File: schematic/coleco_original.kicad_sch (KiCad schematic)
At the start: 6 parts

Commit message: bootup works, controller waits, but no response
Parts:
- added J2: Conn_01x02, Connector_Molex:Molex_KK-254_AE-6410-02A_1x02_P2.54mm_Vertical, symbol Connector_Generic:Conn_01x02
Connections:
- new net GLUE/RX: J2.2 (Pin_2)
- new net GLUE/TX: J2.1 (Pin_1)
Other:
- sheet GLUE ports: added C4_ARM, C7_FIRE, RX, TX; removed none
- sheet controller ports: added C4_ARM, C7_FIRE; removed none
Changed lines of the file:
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@@
+    (stroke (width 0) (type default))
+  )
+  (wire (pts (xy 235.204 109.982) (xy 241.173 109.982))
     (stroke (width 0) (type default))
   )
@@
   )
   (bus (pts (xy 159.258 99.822) (xy 177.165 99.822))
+    (stroke (width 0) (type default))
+  )
+  (wire (pts (xy 235.204 112.141) (xy 241.173 112.141))
     (stroke (width 0) (type default))
   )
@@
         (path "/970e0f64-111f-41e3-9f5a-fb0d0f6fa101"
           (reference "H3") (unit 1)
+        )
+      )
+    )
+  )
+  (symbol (lib_id "Connector_Generic:Conn_01x02") (at 240.284 92.456 0) (unit 1)
+    (in_bom yes) (on_board yes) (dnp no)
+    (property "Reference" "J2" (at 242.316 92.6592 0)
+      (effects (font (size 1.27 1.27)) (justify left))
+    )
+    (property "Value" "Conn_01x02" (at 242.316 94.9706 0)
+      (effects (font (size 1.27 1.27)) (justify left))
+    )
+    (property "Footprint" "Connector_Molex:Molex_KK-254_AE-6410-02A_1x02_P2.54mm_Vertical" (at 240.284 92.456 0)
+      (effects (font (size 1.27 1.27)) hide)
+    )
+    (property "Datasheet" "~" (at 240.284 92.456 0)
+      (effects (font (size 1.27 1.27)) hide)
+    )
+    (pin "1")
+    (pin "2")
+    (instances
+      (project "coleco_original"
+        (path "/970e0f64-111f-41e3-9f5a-fb0d0f6fa101/00000000-0000-0000-0000-000062624749"
+          (reference "J2") (unit 1)
+        )
+        (path "/970e0f64-111f-41e3-9f5a-fb0d0f6fa101"
+          (reference "J9") (unit 1)
+        )
+      )
+      (project "picerino_sn76489AN"
+        (path "/b5352a33-563a-4ffe-a231-2e68fb54afa3"
+          (reference "J2") (unit 1)
         )
       )
@@
       (effects (font (size 1.27 1.27)) (justify left))
     )
+    (pin "RX" input (at 235.204 94.996 0)
+      (effects (font (size 1.27 1.27)) (justify right))
+    )
+    (pin "TX" output (at 235.204 92.456 0)
+      (effects (font (size 1.27 1.27)) (justify right))
+    )
+    (pin "C4_ARM" output (at 235.204 109.982 0)
+      (effects (font (size 1.27 1.27)) (justify right))
+    )
+    (pin "C7_FIRE" output (at 235.204 112.141 0)
+      (effects (font (size 1.27 1.27)) (justify right))
+    )
     (instances
       (project "coleco_original"
@@
       (effects (font (size 1.27 1.27)) (justify left))
     )
+    (pin "C4_ARM" input (at 241.173 109.982 180)
+      (effects (font (size 1.27 1.27)) (justify left))
+    )
+    (pin "C7_FIRE" input (at 241.173 112.141 180)
+      (effects (font (size 1.27 1.27)) (justify left))
+    )

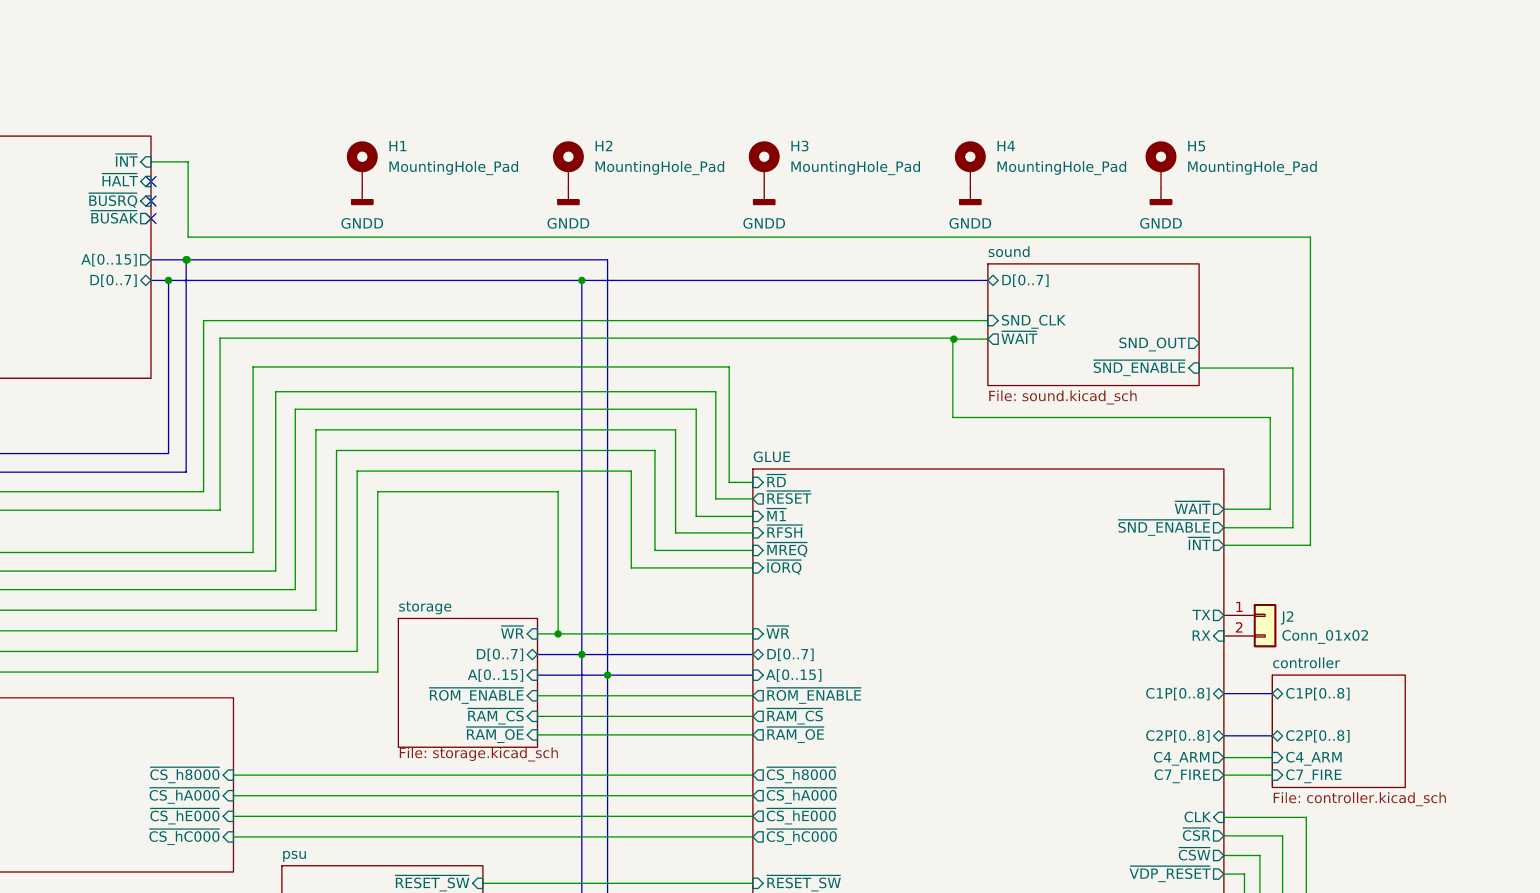
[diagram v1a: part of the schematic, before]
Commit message: added volume and adjusted cart port
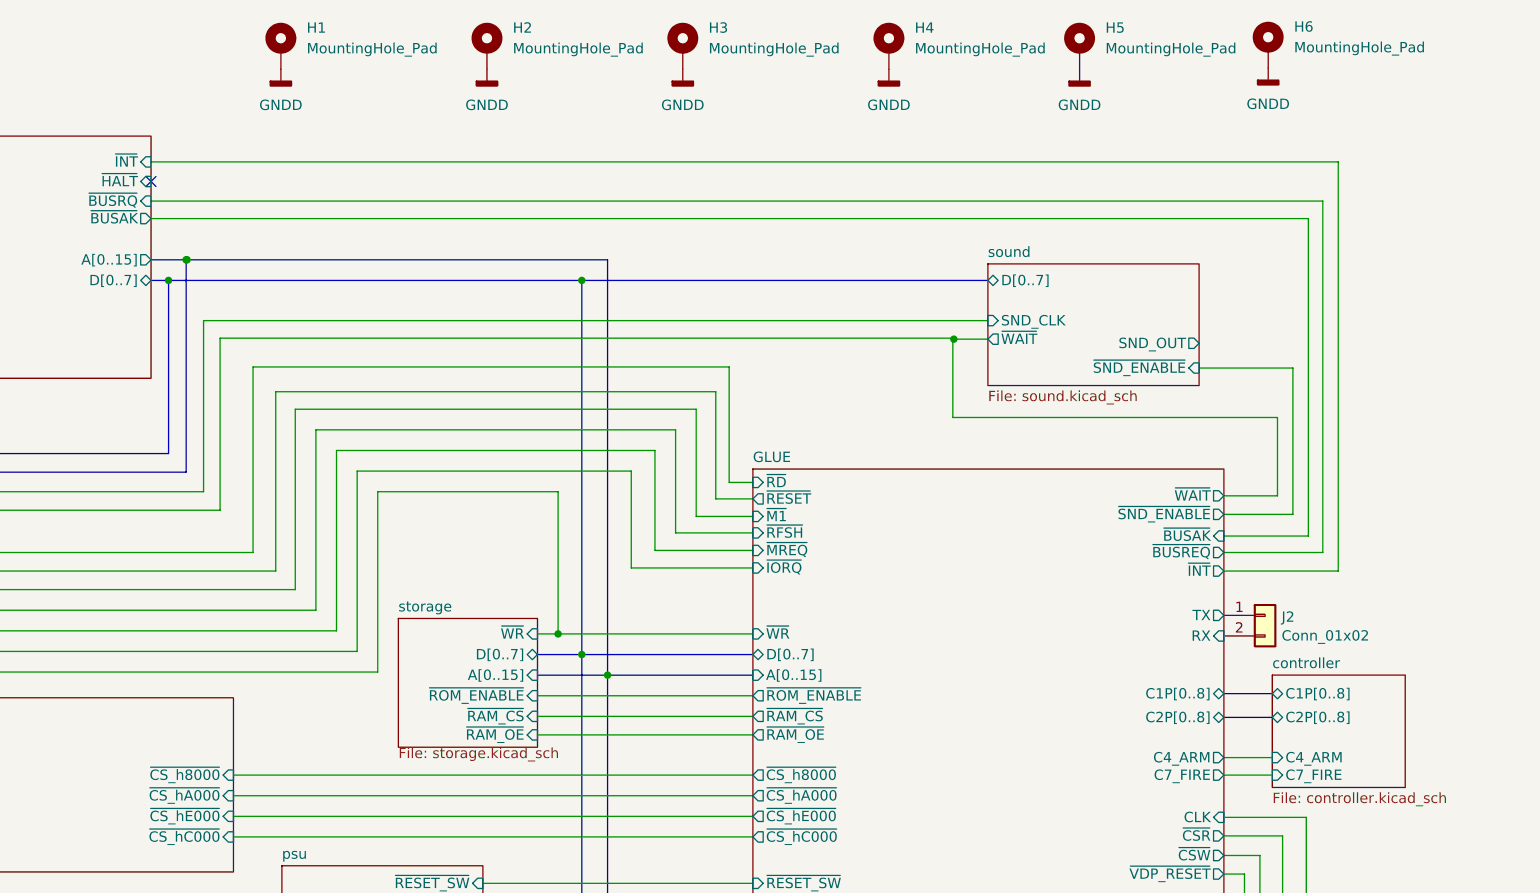
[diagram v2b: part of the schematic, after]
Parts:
- added H6: MountingHole_Pad, MountingHole:MountingHole_3.2mm_M3_DIN965_Pad, symbol Mechanical:MountingHole_Pad
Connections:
- net GNDD: now also H6.1
- no-connect marks 3 -> 1
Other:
- sheet GLUE ports: added ~{BUSAK}, ~{BUSREQ}; removed none
- moved on the sheet: H1, H2, H3, H4, H5

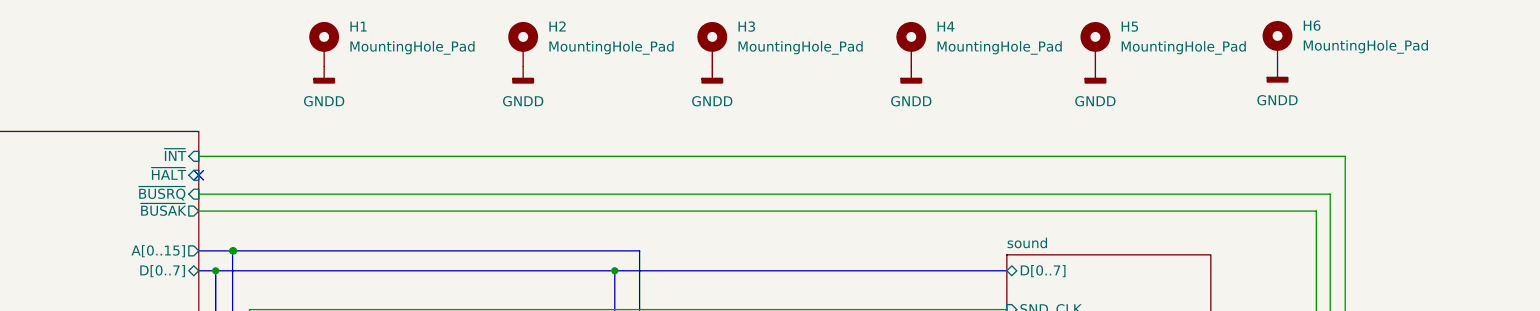
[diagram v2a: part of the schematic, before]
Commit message: first iteration of version v1. PCB placed, checked but needs final go through and case design before send out.
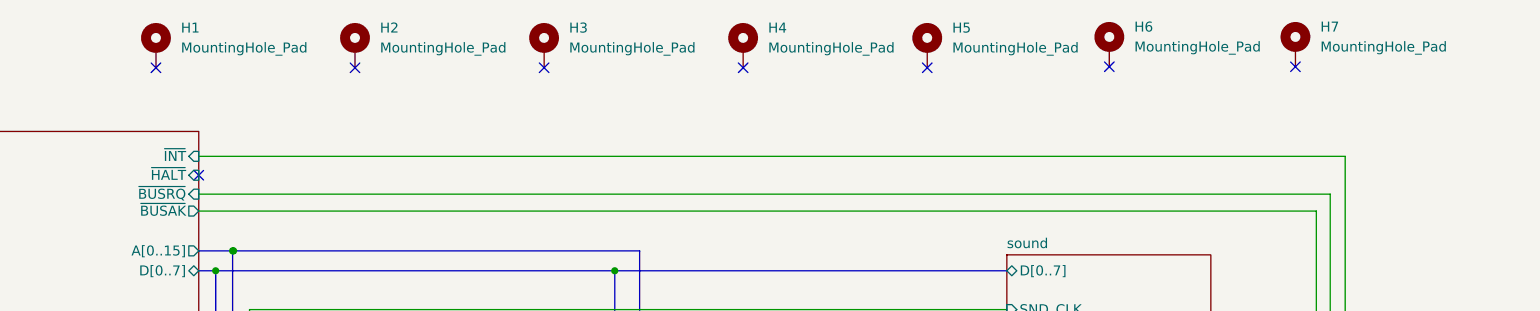
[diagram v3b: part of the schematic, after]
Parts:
- added H7: MountingHole_Pad, MountingHole:MountingHole_3.2mm_M3_DIN965_Pad, symbol Mechanical:MountingHole_Pad
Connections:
- removed net GNDD: H1.1, H2.1, H3.1, H4.1, H5.1, H6.1
- no-connect marks 1 -> 8
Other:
- moved on the sheet: H1, H2, H3, H4, H5, H6

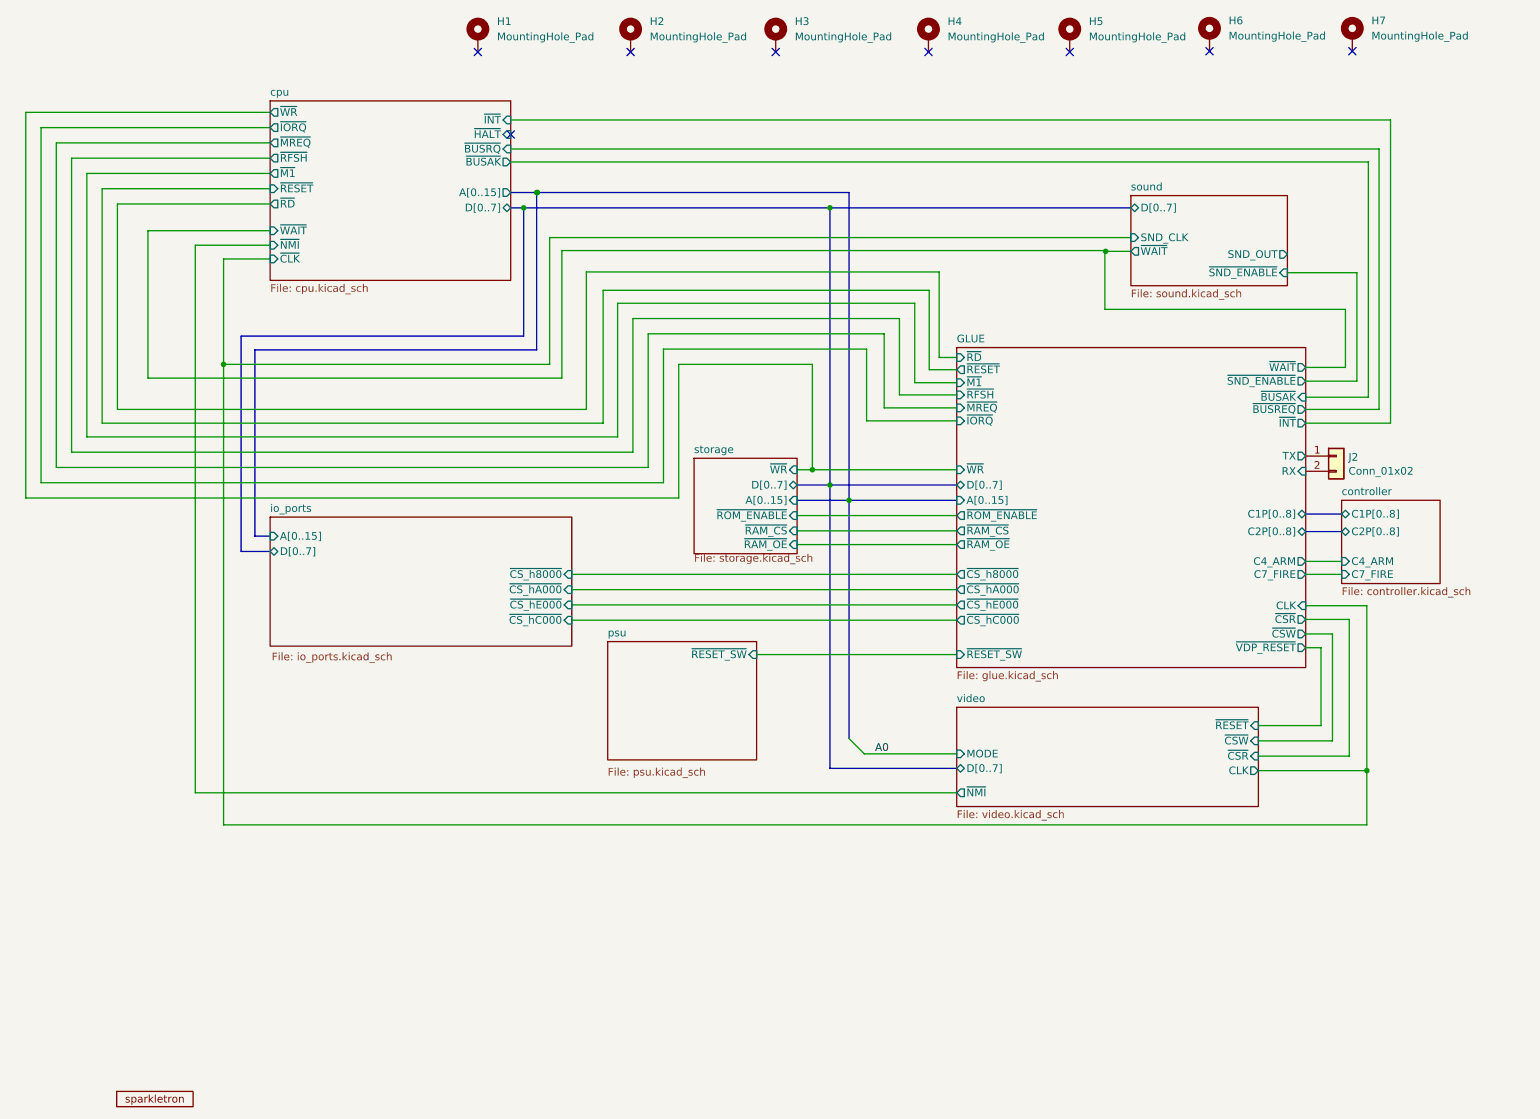
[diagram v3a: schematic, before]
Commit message: added power port for lcd and adjusted board traces and fill
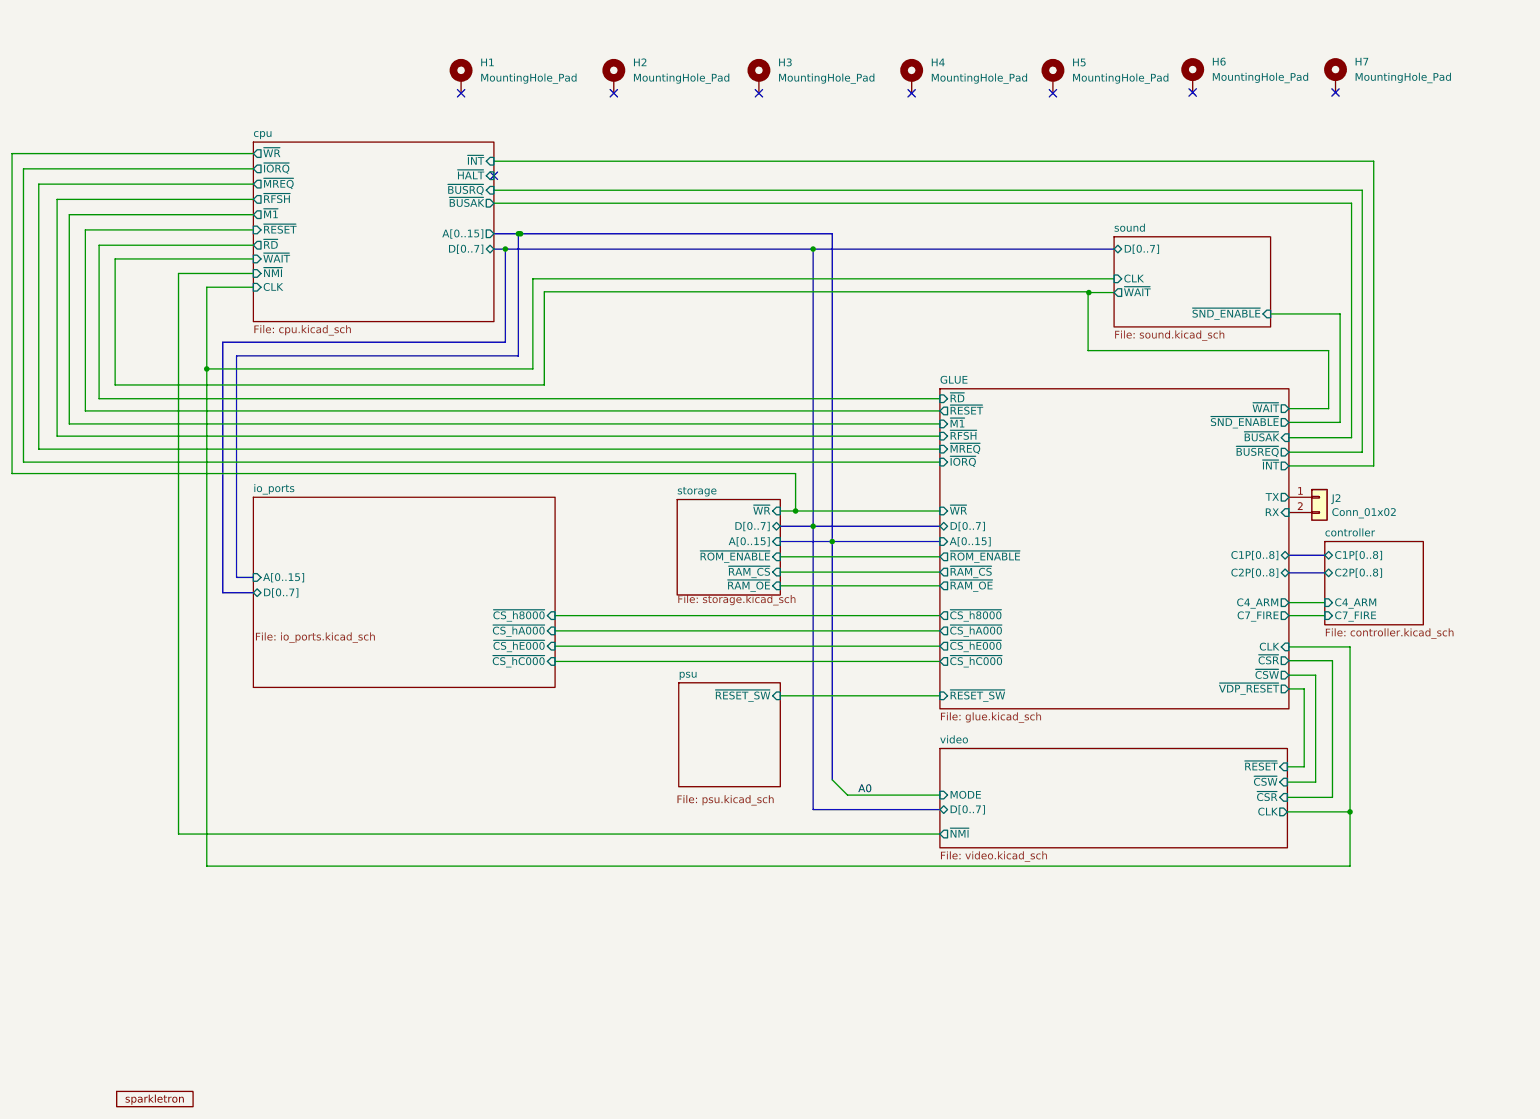
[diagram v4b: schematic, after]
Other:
- sheet cpu ports: added CLK; removed ~{CLK}
- sheet sound ports: added CLK; removed SND_CLK, SND_OUT
- moved on the sheet: H1, H2, H3, H4, H5, H6, H7, J2
